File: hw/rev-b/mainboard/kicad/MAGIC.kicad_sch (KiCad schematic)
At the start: 16 parts, among them U7 SN74LVC4245APWR, U8 SN74LVC4245APWR, U9 SN74LVC4245APWR

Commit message: chore(hw): tidy MAGIC schematic
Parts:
- U7, U8, U9: value SN74LVC4245APWR -> SN74LVC4245A
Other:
- moved on the sheet: C32, C33, C34, C35, C36, C37, C38

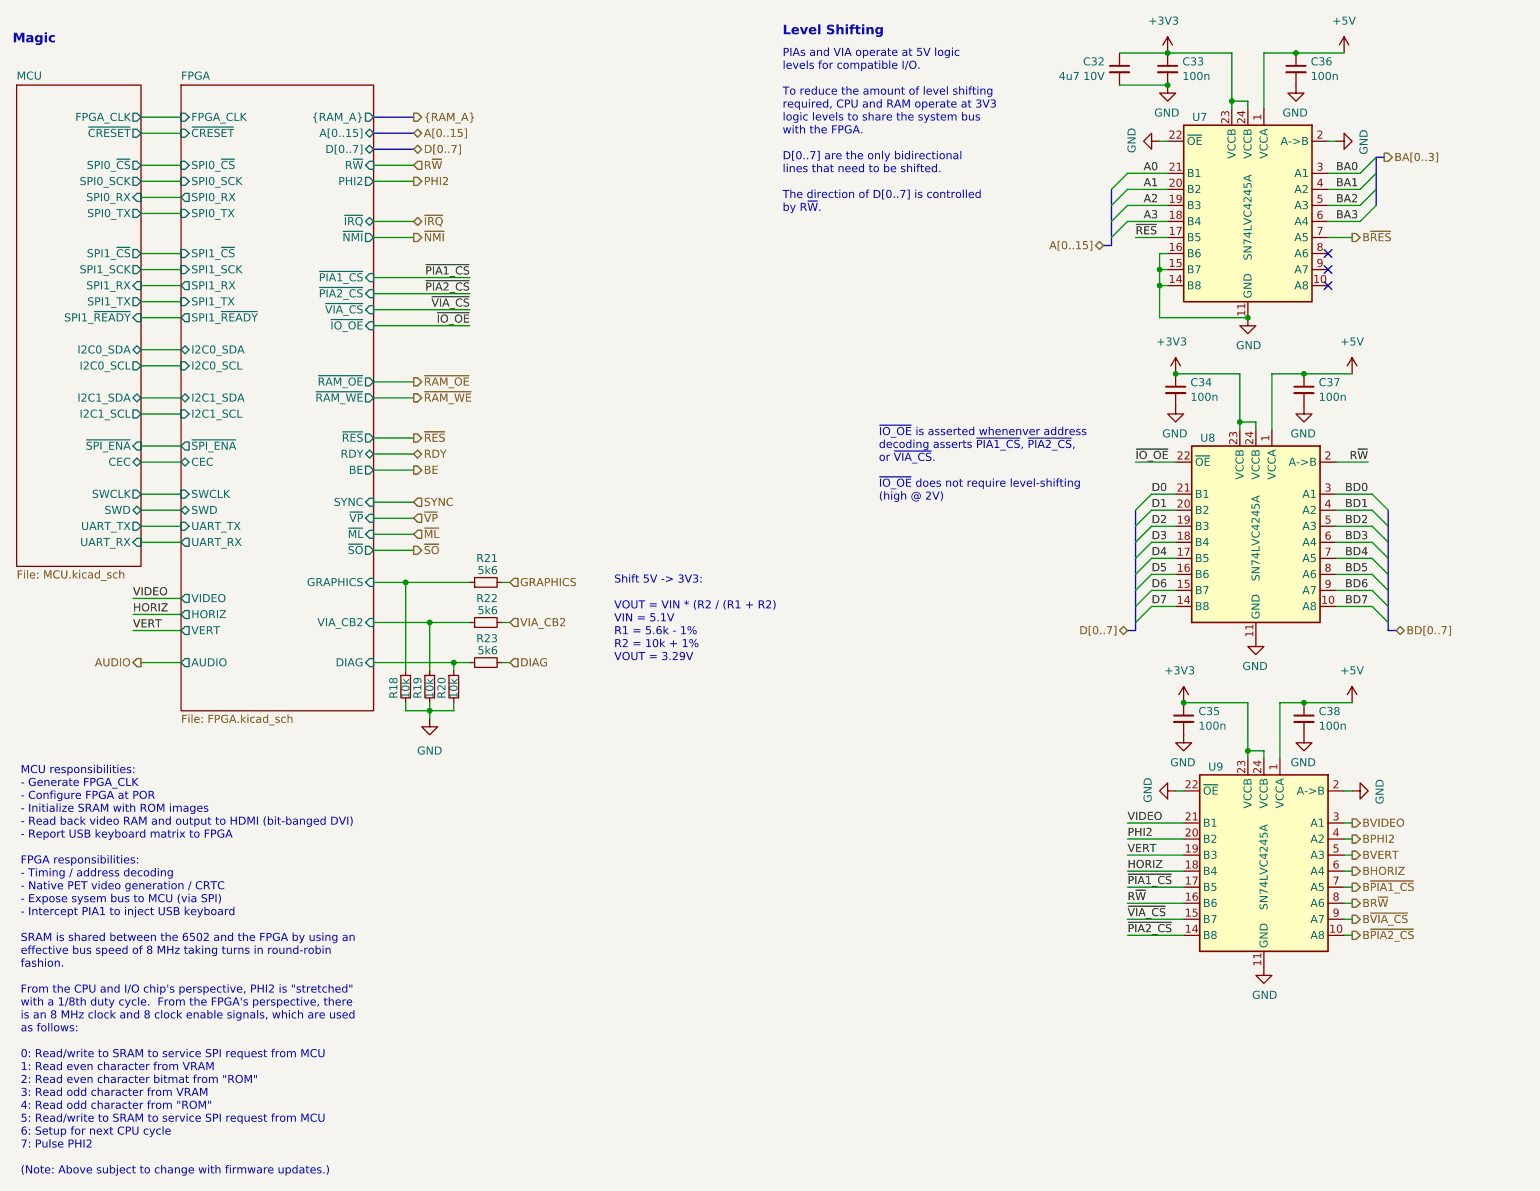
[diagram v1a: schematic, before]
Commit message: hw: repurpose SP0 (spare) for independent VSYNC
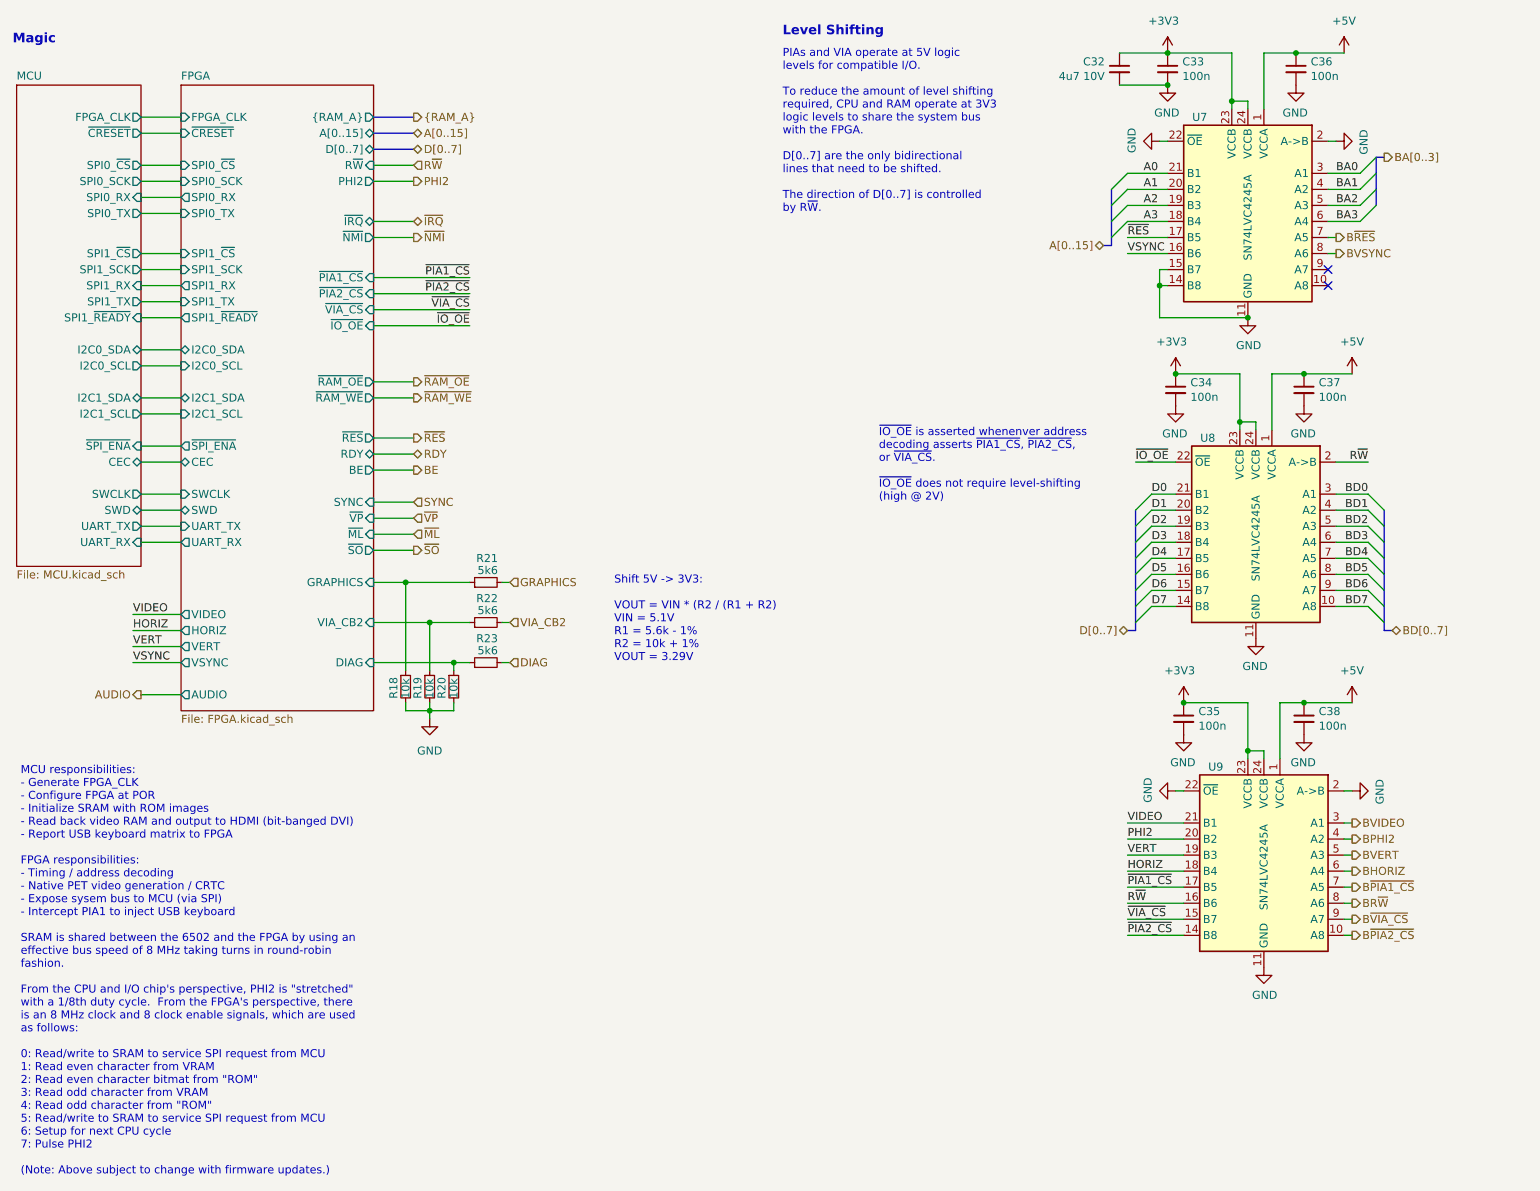
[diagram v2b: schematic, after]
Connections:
- net GND: no longer U7.16 (B6)
- net BVSYNC: now reaches U7.8 (A6)
- new net VSYNC: U7.16 (B6)
- no-connect marks 3 -> 2
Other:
- sheet FPGA ports: added VSYNC; removed none
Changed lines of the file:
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@@
 	)
 	(junction
-		(at 207.01 54.61)
-		(diameter 0)
-		(color 0 0 0 0)
-	)
-	(junction
 		(at 228.6 20.32)
 		(diameter 0)
@@
 	)
 	(no_connect
-		(at 233.68 52.07)
-	)
-	(no_connect
 		(at 233.68 54.61)
 	)
@@
 	)
 	(bus_entry
-		(at 240.665 90.17)
+		(at 240.03 90.17)
 		(size 2.54 2.54)
 		(stroke
@@
 	)
 	(bus_entry
-		(at 240.665 97.79)
+		(at 240.03 97.79)
 		(size 2.54 2.54)
 		(stroke
@@
 	)
 	(bus_entry
-		(at 240.665 92.71)
+		(at 240.03 92.71)
 		(size 2.54 2.54)
 		(stroke
@@
 	)
 	(bus_entry
-		(at 240.665 107.95)
+		(at 240.03 107.95)
 		(size 2.54 2.54)
 		(stroke
@@
 	)
 	(bus_entry
-		(at 240.665 105.41)
+		(at 240.03 105.41)
 		(size 2.54 2.54)
 		(stroke
@@
 	)
 	(bus_entry
-		(at 240.665 100.33)
+		(at 240.03 100.33)
 		(size 2.54 2.54)
 		(stroke
@@
 	)
 	(bus_entry
-		(at 240.665 102.87)
+		(at 240.03 102.87)
 		(size 2.54 2.54)
 		(stroke
@@
 	)
 	(bus_entry
-		(at 240.665 95.25)
+		(at 240.03 95.25)
 		(size 2.54 2.54)
 		(stroke
@@
 	(wire
 		(pts
-			(xy 240.665 90.17) (xy 234.95 90.17)
+			(xy 240.03 90.17) (xy 234.95 90.17)
 		)
 		(stroke
@@
 	(bus
 		(pts
-			(xy 243.205 102.87) (xy 243.205 105.41)
+			(xy 242.57 102.87) (xy 242.57 105.41)
 		)
 		(stroke
@@
 	(wire
 		(pts
-			(xy 234.95 100.33) (xy 240.665 100.33)
+			(xy 234.95 100.33) (xy 240.03 100.33)
 		)
 		(stroke
@@
 	(wire
 		(pts
-			(xy 234.95 105.41) (xy 240.665 105.41)
+			(xy 234.95 105.41) (xy 240.03 105.41)
 		)
 		(stroke
@@
 	(wire
 		(pts
-			(xy 208.28 49.53) (xy 203.2 49.53)
+			(xy 208.28 49.53) (xy 201.93 49.53)
 		)
 		(stroke
@@
 	(wire
 		(pts
-			(xy 208.28 52.07) (xy 207.01 52.07)
-		)
-		(stroke
-			(width 0)
-			(type default)
-		)
-	)
-	(wire
-		(pts
 			(xy 208.28 39.37) (xy 201.93 39.37)
 		)
@@
 	(bus
 		(pts
-			(xy 243.205 92.71) (xy 243.205 95.25)
+			(xy 242.57 92.71) (xy 242.57 95.25)
 		)
 		(stroke
@@
 	(bus
 		(pts
-			(xy 243.205 105.41) (xy 243.205 107.95)
+			(xy 242.57 105.41) (xy 242.57 107.95)
 		)
 		(stroke
@@
 	(bus
 		(pts
-			(xy 243.205 97.79) (xy 243.205 100.33)
+			(xy 242.57 97.79) (xy 242.57 100.33)
 		)
 		(stroke
@@
 	(bus
 		(pts
-			(xy 244.475 111.76) (xy 243.205 111.76)
+			(xy 243.84 111.76) (xy 242.57 111.76)
+		)
+		(stroke
+			(width 0)
+			(type default)
+		)
+	)
+	(wire
+		(pts
+			(xy 208.28 52.07) (xy 201.93 52.07)
 		)
 		(stroke
@@
 	(wire
 		(pts
-			(xy 234.95 107.95) (xy 240.665 107.95)
+			(xy 234.95 107.95) (xy 240.03 107.95)
 		)
 		(stroke
@@
 	(wire
 		(pts
-			(xy 240.665 97.79) (xy 234.95 97.79)
+			(xy 240.03 97.79) (xy 234.95 97.79)
 		)
 		(stroke
@@
 	(wire
 		(pts
-			(xy 234.95 102.87) (xy 240.665 102.87)
+			(xy 234.95 102.87) (xy 240.03 102.87)
 		)
 		(stroke
@@
 	(wire
 		(pts
-			(xy 240.665 92.71) (xy 234.95 92.71)
+			(xy 240.03 92.71) (xy 234.95 92.71)
 		)
 		(stroke
@@
 	(wire
 		(pts
-			(xy 52.07 111.76) (xy 44.45 111.76)
+			(xy 52.07 114.3) (xy 44.45 114.3)
 		)
 		(stroke
@@
 	(bus
 		(pts
-			(xy 243.205 95.25) (xy 243.205 97.79)
+			(xy 242.57 95.25) (xy 242.57 97.79)
 		)
 		(stroke
@@
 	(wire
 		(pts
-			(xy 240.665 95.25) (xy 234.95 95.25)
+			(xy 240.03 95.25) (xy 234.95 95.25)
 		)
 		(stroke
@@
 	(wire
 		(pts
-			(xy 45.72 116.84) (xy 52.07 116.84)
+			(xy 45.72 121.92) (xy 52.07 121.92)
 		)
 		(stroke
@@
 	(bus
 		(pts
-			(xy 243.205 110.49) (xy 243.205 111.76)
+			(xy 242.57 110.49) (xy 242.57 111.76)
+		)
+		(stroke
+			(width 0)
+			(type default)
+		)
+	)
+	(wire
+		(pts
+			(xy 52.07 116.84) (xy 44.45 116.84)
 		)
 		(stroke
@@
 	(wire
 		(pts
-			(xy 52.07 109.22) (xy 44.45 109.22)
+			(xy 52.07 111.76) (xy 44.45 111.76)
 		)
 		(stroke
@@
 	(wire
 		(pts
+			(xy 233.68 52.07) (xy 234.95 52.07)
+		)
+		(stroke
+			(width 0)
+			(type default)
+		)
+	)
+	(wire
+		(pts
 			(xy 45.72 74.93) (xy 52.07 74.93)
 		)
@@
 		)
 	)
-	(wire
-		(pts
-			(xy 207.01 52.07) (xy 207.01 54.61)
-		)
-		(stroke
-			(width 0)
-			(type default)
-		)
-	)
 	(bus
 		(pts
-			(xy 243.205 107.95) (xy 243.205 110.49)
+			(xy 242.57 107.95) (xy 242.57 110.49)
 		)
 		(stroke
@@
 	(wire
 		(pts
-			(xy 52.07 106.68) (xy 44.45 106.68)
+			(xy 52.07 109.22) (xy 44.45 109.22)
 		)
 		(stroke
@@
 	(bus
 		(pts
-			(xy 243.205 100.33) (xy 243.205 102.87)
+			(xy 242.57 100.33) (xy 242.57 102.87)
 		)
 		(stroke
@@
 	(wire
 		(pts
-			(xy 233.68 49.53) (xy 237.49 49.53)
+			(xy 233.68 49.53) (xy 234.95 49.53)
 		)
 		(stroke
@@
 		)
 	)
+	(label "VSYNC"
+		(at 44.45 116.84 0)
+		(fields_autoplaced yes)
+		(effects
+			(font
+				(size 1.27 1.27)
+			)
+			(justify left bottom)
+		)
+	)
 	(label "~{IO_OE}"
 		(at 97.79 63.5 180)
@@
 	)
 	(label "~{RES}"
-		(at 203.2 49.53 0)
+		(at 201.93 49.53 0)
 		(fields_autoplaced yes)
 		(effects
@@
 	)
 	(label "HORIZ"
-		(at 44.45 109.22 0)
+		(at 44.45 111.76 0)
 		(fields_autoplaced yes)
 		(effects
@@
 		)
 	)
+	(label "VSYNC"
+		(at 201.93 52.07 0)
+		(fields_autoplaced yes)
+		(effects
+			(font
+				(size 1.27 1.27)
+			)
+			(justify left bottom)
+		)
+	)
 	(label "BD3"
 		(at 240.03 97.79 180)
@@
 	)
 	(label "VERT"
-		(at 44.45 111.76 0)
+		(at 44.45 114.3 0)
 		(fields_autoplaced yes)
 		(effects
@@
 	)
 	(label "VIDEO"
-		(at 44.45 106.68 0)
+		(at 44.45 109.22 0)
 		(fields_autoplaced yes)
 		(effects
@@
 		)
 	)
+	(hierarchical_label "BVSYNC"
+		(shape output)
+		(at 234.95 52.07 0)
+		(fields_autoplaced yes)
+		(effects
+			(font
+				(size 1.27 1.27)
+			)
+			(justify left)
+		)
+	)
 	(hierarchical_label "~{NMI}"
 		(shape output)
@@
 	(hierarchical_label "B~{RES}"
 		(shape output)
-		(at 237.49 49.53 0)
+		(at 234.95 49.53 0)
 		(fields_autoplaced yes)
 		(effects
@@
 	(hierarchical_label "AUDIO"
 		(shape output)
-		(at 45.72 116.84 180)
+		(at 45.72 121.92 180)
 		(fields_autoplaced yes)
 		(effects
@@
 	(hierarchical_label "BD[0..7]"
 		(shape bidirectional)
-		(at 244.475 111.76 0)
+		(at 243.84 111.76 0)
 		(fields_autoplaced yes)
 		(effects
@@
 		)
 		(pin "VERT" output
-			(at 52.07 111.76 180)
+			(at 52.07 114.3 180)
 			(effects
 				(font
@@
 		)
 		(pin "HORIZ" output
-			(at 52.07 109.22 180)
+			(at 52.07 111.76 180)
 			(effects
 				(font
@@
 		)
 		(pin "VIDEO" output
-			(at 52.07 106.68 180)
+			(at 52.07 109.22 180)
 			(effects
 				(font
@@
 		)
 		(pin "AUDIO" output
+			(at 52.07 121.92 180)
+			(effects
+				(font
+					(size 1.27 1.27)
+				)
+				(justify left)
+			)
+		)
+		(pin "VSYNC" output
 			(at 52.07 116.84 180)
 			(effects

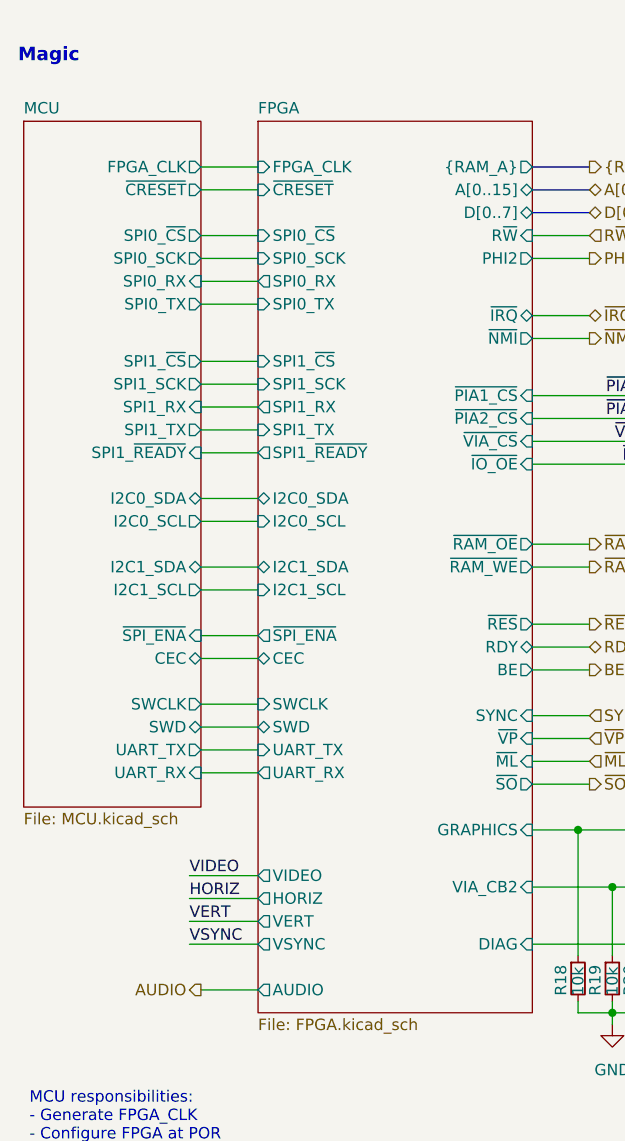
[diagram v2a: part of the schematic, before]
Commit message: hw: audio_det, stitching around sram
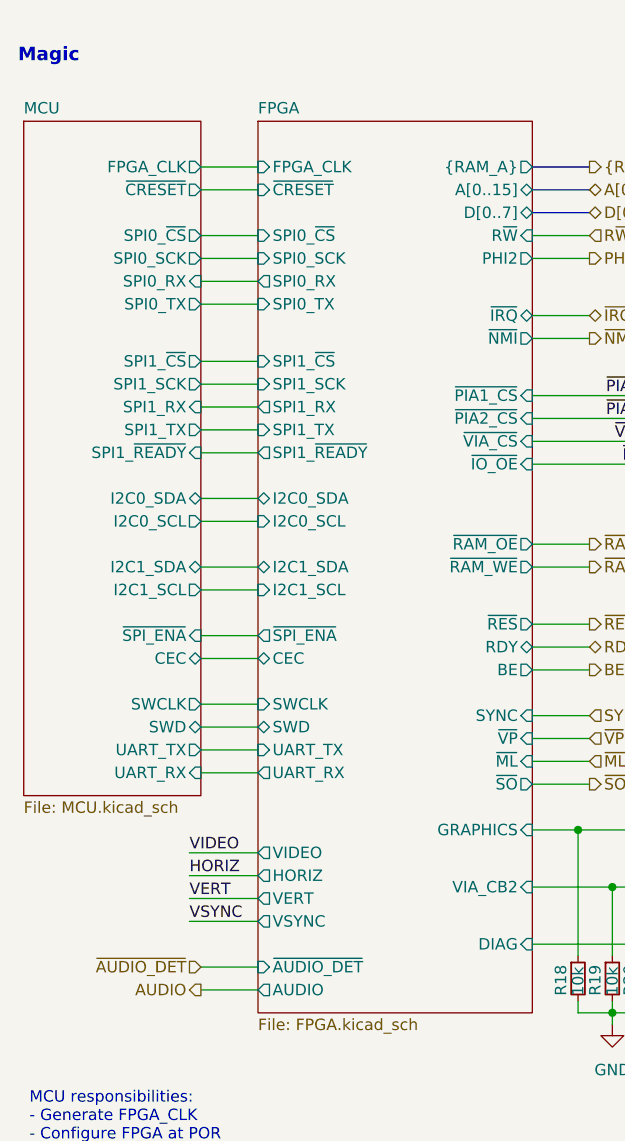
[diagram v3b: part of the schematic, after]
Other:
- sheet FPGA ports: added ~{AUDIO_DET}; removed none
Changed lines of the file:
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@@
 	(wire
 		(pts
-			(xy 52.07 114.3) (xy 44.45 114.3)
+			(xy 52.07 111.76) (xy 44.45 111.76)
 		)
 		(stroke
@@
 	(wire
 		(pts
+			(xy 45.72 119.38) (xy 52.07 119.38)
+		)
+		(stroke
+			(width 0)
+			(type default)
+		)
+	)
+	(wire
+		(pts
 			(xy 233.68 41.91) (xy 238.76 41.91)
 		)
@@
 	(wire
 		(pts
-			(xy 52.07 116.84) (xy 44.45 116.84)
+			(xy 52.07 114.3) (xy 44.45 114.3)
 		)
 		(stroke
@@
 	(wire
 		(pts
-			(xy 52.07 111.76) (xy 44.45 111.76)
+			(xy 52.07 109.22) (xy 44.45 109.22)
 		)
 		(stroke
@@
 	(wire
 		(pts
-			(xy 52.07 109.22) (xy 44.45 109.22)
+			(xy 52.07 106.68) (xy 44.45 106.68)
 		)
 		(stroke
@@
 	)
 	(label "VSYNC"
-		(at 44.45 116.84 0)
+		(at 44.45 114.3 0)
 		(fields_autoplaced yes)
 		(effects
@@
 	)
 	(label "HORIZ"
-		(at 44.45 111.76 0)
+		(at 44.45 109.22 0)
 		(fields_autoplaced yes)
 		(effects
@@
 	)
 	(label "VERT"
-		(at 44.45 114.3 0)
+		(at 44.45 111.76 0)
 		(fields_autoplaced yes)
 		(effects
@@
 	)
 	(label "VIDEO"
-		(at 44.45 109.22 0)
+		(at 44.45 106.68 0)
 		(fields_autoplaced yes)
 		(effects
@@
 		)
 	)
+	(hierarchical_label "~{AUDIO_DET}"
+		(shape input)
+		(at 45.72 119.38 180)
+		(fields_autoplaced yes)
+		(effects
+			(font
+				(size 1.27 1.27)
+			)
+			(justify right)
+		)
+	)
 	(hierarchical_label "BE"
 		(shape output)
@@
 		)
 		(pin "VERT" output
-			(at 52.07 114.3 180)
+			(at 52.07 111.76 180)
 			(effects
 				(font
@@
 		)
 		(pin "HORIZ" output
-			(at 52.07 111.76 180)
+			(at 52.07 109.22 180)
 			(effects
 				(font
@@
 		)
 		(pin "VIDEO" output
-			(at 52.07 109.22 180)
+			(at 52.07 106.68 180)
 			(effects
 				(font
@@
 		)
 		(pin "VSYNC" output
-			(at 52.07 116.84 180)
+			(at 52.07 114.3 180)
+			(effects
+				(font
+					(size 1.27 1.27)
+				)
+				(justify left)
+			)
+		)
+		(pin "~{AUDIO_DET}" input
+			(at 52.07 119.38 180)
 			(effects
 				(font
@@
 	(sheet
 		(at 26.035 25.4)
-		(size 19.685 76.2)
+		(size 19.685 74.93)
 		(fields_autoplaced yes)
 		(stroke
@@
 		)
 		(property "Sheetfile" "MCU.kicad_sch"
-			(at 26.035 102.1846 0)
+			(at 26.035 100.9146 0)
 			(effects
 				(font
